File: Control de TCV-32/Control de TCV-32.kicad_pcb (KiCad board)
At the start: 2 copper layers, 6 parts, among them J1 Bocina, J2 Microfono, J3 Screw_Terminal_01x02, J5 HC-05, U1 LM7805_TO220

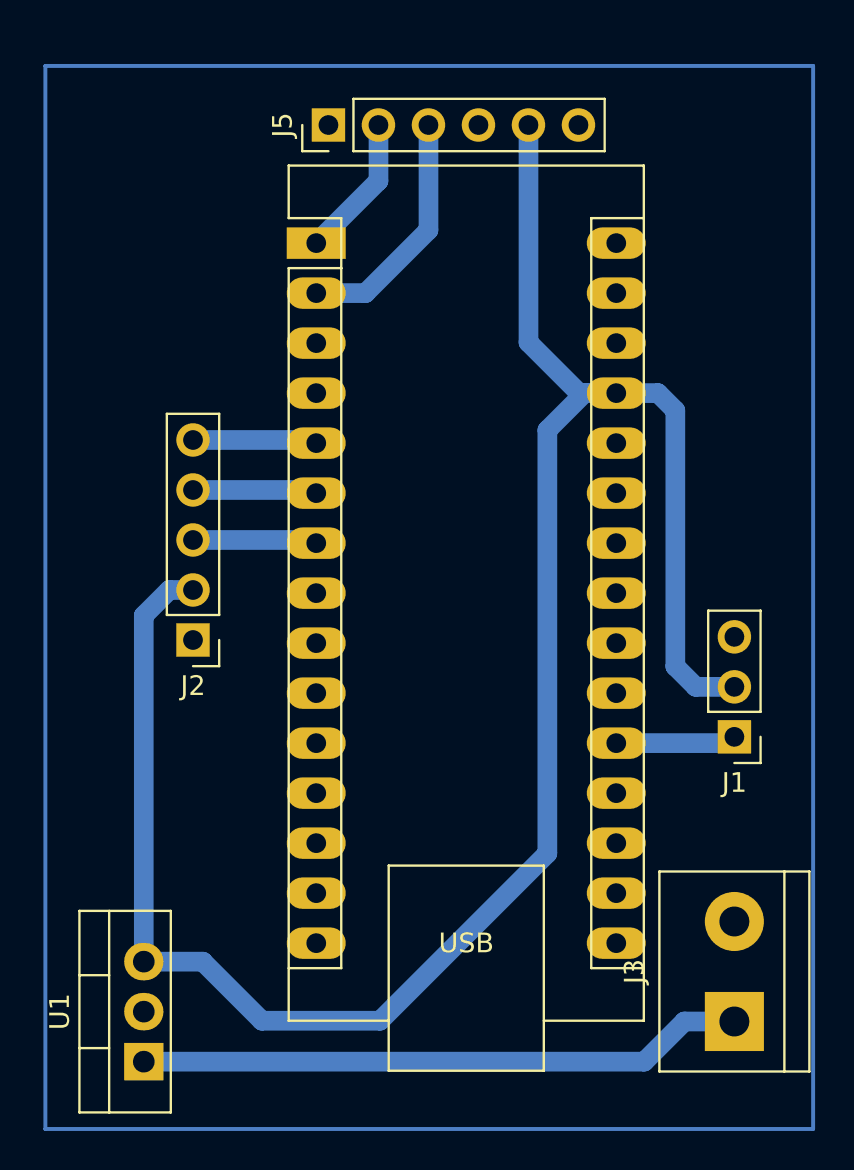
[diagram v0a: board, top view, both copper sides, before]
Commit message: Cambio de componentes
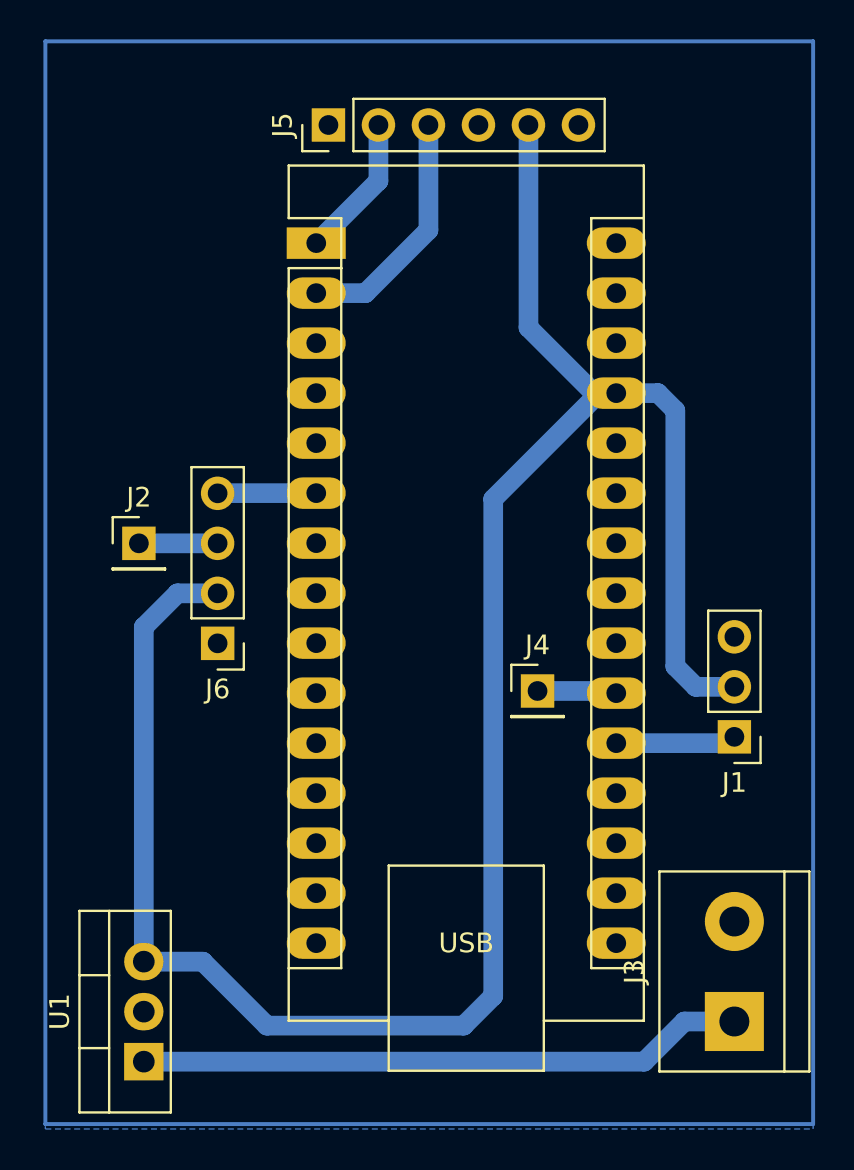
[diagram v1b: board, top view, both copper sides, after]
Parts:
- added J4: Conn_01x01_Pin, Connector_PinHeader_2.54mm:PinHeader_1x01_P2.54mm_Vertical, F.Cu at (185.5, 65.2)
- added J6: Conn_01x04_Pin, Connector_PinHeader_2.54mm:PinHeader_1x04_P2.54mm_Vertical, F.Cu at (169.2, 62.8)
- J2: value Microfono -> Conn_01x01_Pin; footprint Connector_PinHeader_2.54mm:PinHeader_1x05_P2.54mm_Vertical -> Connector_PinHeader_2.54mm:PinHeader_1x01_P2.54mm_Vertical
- moved J2 5.63 mm to (165.2, 57.8), turned to 0 degrees
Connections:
- A2 pad 21: unconnected-(A2-A2-Pad21) -> Aout
- A2 pad 5: Atack -> unconnected-(A2-D2-Pad5)
- A2 pad 6: OUT -> Dout
- A2 pad 7: GAIN -> unconnected-(A2-D4-Pad7)
- J2 pad 1: GND -> 1
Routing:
- net OUT: track 6.33 -> 0.00 mm
- net GAIN: track 6.33 -> 0.00 mm
- net Atack: track 6.33 -> 0.00 mm
- net Dout: track 0.00 -> 5.24 mm
- net Aout: track 0.00 -> 4.05 mm
- net 1: track 0.00 -> 4.00 mm
- net +5V: track 108.0 -> 110.8 mm

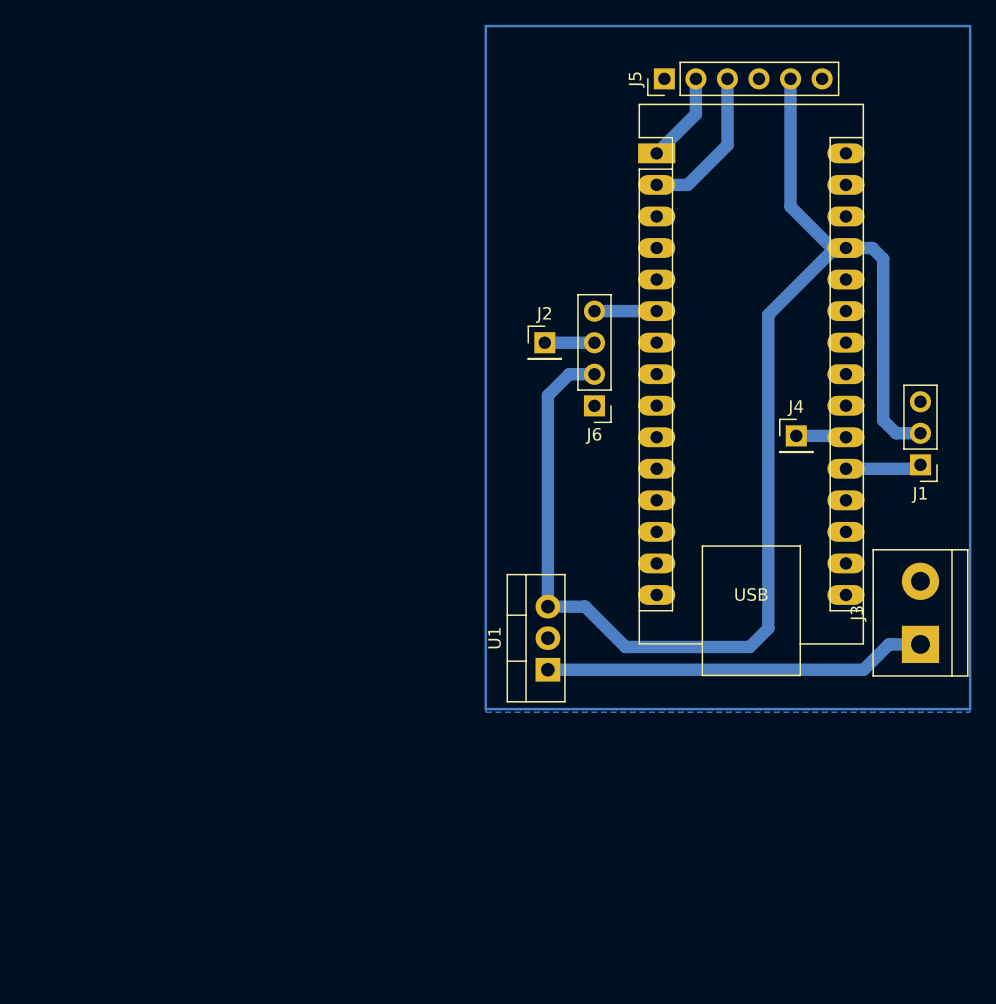
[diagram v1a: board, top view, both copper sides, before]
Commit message: Placa C modificada con ESP32 C3
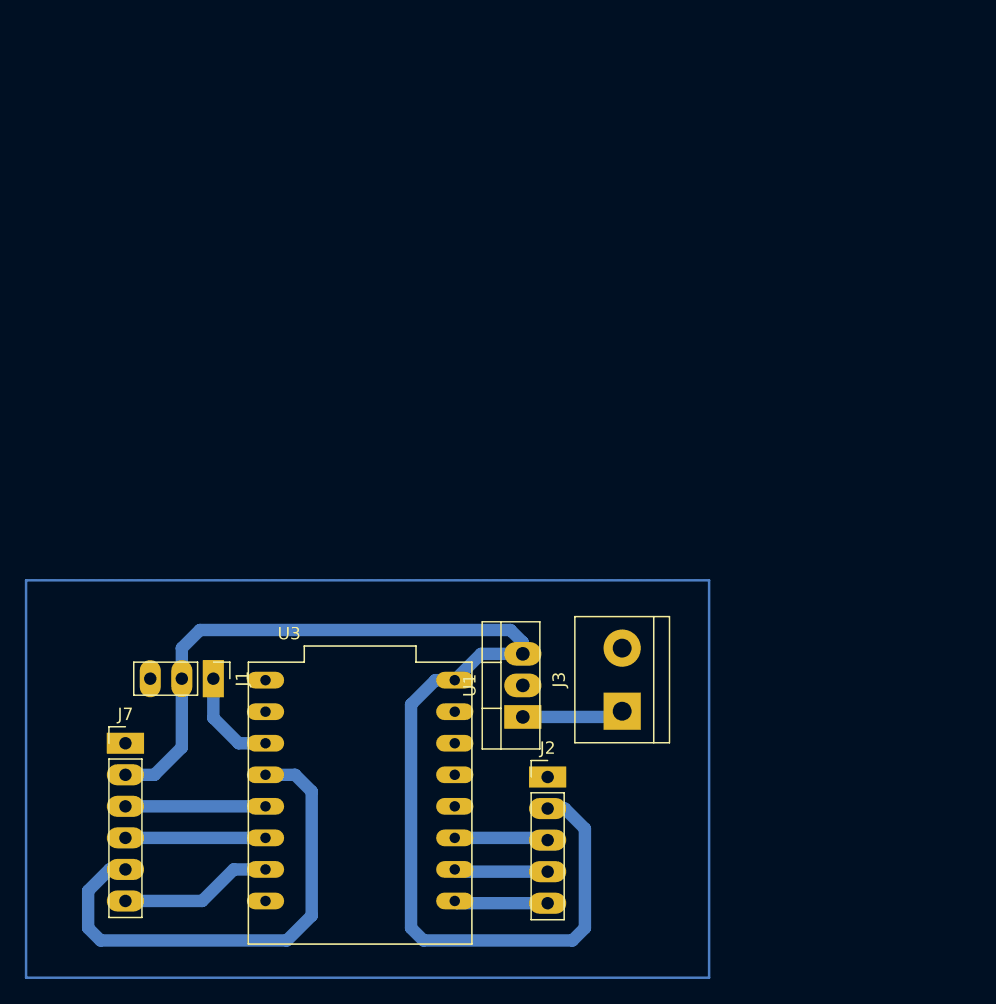
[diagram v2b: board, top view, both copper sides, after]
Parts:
- removed A2: Arduino_Nano_v3.x, Module:Arduino_Nano
- removed J4: Conn_01x01_Pin, Connector_PinHeader_2.54mm:PinHeader_1x01_P2.54mm_Vertical
- removed J5: HC-05, Connector_PinHeader_2.54mm:PinHeader_1x06_P2.54mm_Vertical
- removed J6: Conn_01x04_Pin, Connector_PinHeader_2.54mm:PinHeader_1x04_P2.54mm_Vertical
- added J7: SD, Connector_PinHeader_2.54mm:PinHeader_1x06_P2.54mm_Vertical, F.Cu at (131.5, 90.0)
- added U3: ESP32-C3_SUPERMINI_TH, huellas:MODULE_ESP32-C3_SUPERMINI_TH, F.Cu at (150.4, 94.8)
- J2: value Conn_01x01_Pin -> MAX9814; footprint Connector_PinHeader_2.54mm:PinHeader_1x01_P2.54mm_Vertical -> Connector_PinHeader_2.54mm:PinHeader_1x05_P2.54mm_Vertical
- moved J1 59.5 mm to (138.6, 84.8), turned to -90 degrees
- moved J2 35.0 mm to (165.5, 92.7)
- moved J3 24.6 mm to (171.5, 87.4)
- moved U1 4.30 mm to (163.5, 87.9)
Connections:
- J2 pad 1: 1 -> GND
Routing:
- net SCK: track 0.00 -> 40.2 mm
- net VCC: track 30.8 -> 8.19 mm
- net +5V: track 110.8 -> 98.0 mm
- net TXD: track 12.4 -> 0.00 mm
- net CS: track 0.00 -> 12.3 mm
- net MOSI: track 0.00 -> 11.3 mm
- net MISO: track 0.00 -> 11.3 mm
- net OUT: track 0.00 -> 7.55 mm
- net Gain: track 0.00 -> 7.55 mm
- net AR: track 0.00 -> 7.55 mm
- net RXD: track 7.31 -> 0.00 mm
- net Dout: track 5.24 -> 0.00 mm
- net Aout: track 4.05 -> 0.00 mm
- net 1: track 4.00 -> 0.00 mm
- net L3output: track 6.13 -> 8.20 mm
